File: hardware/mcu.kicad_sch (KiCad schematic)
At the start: 34 parts, among them J37 Micro_SD_Card, J38 Micro_SD_Card, U4 W25Q32JVZP, U5 RP2040, Y1 12 MHz ABM8-272-T3

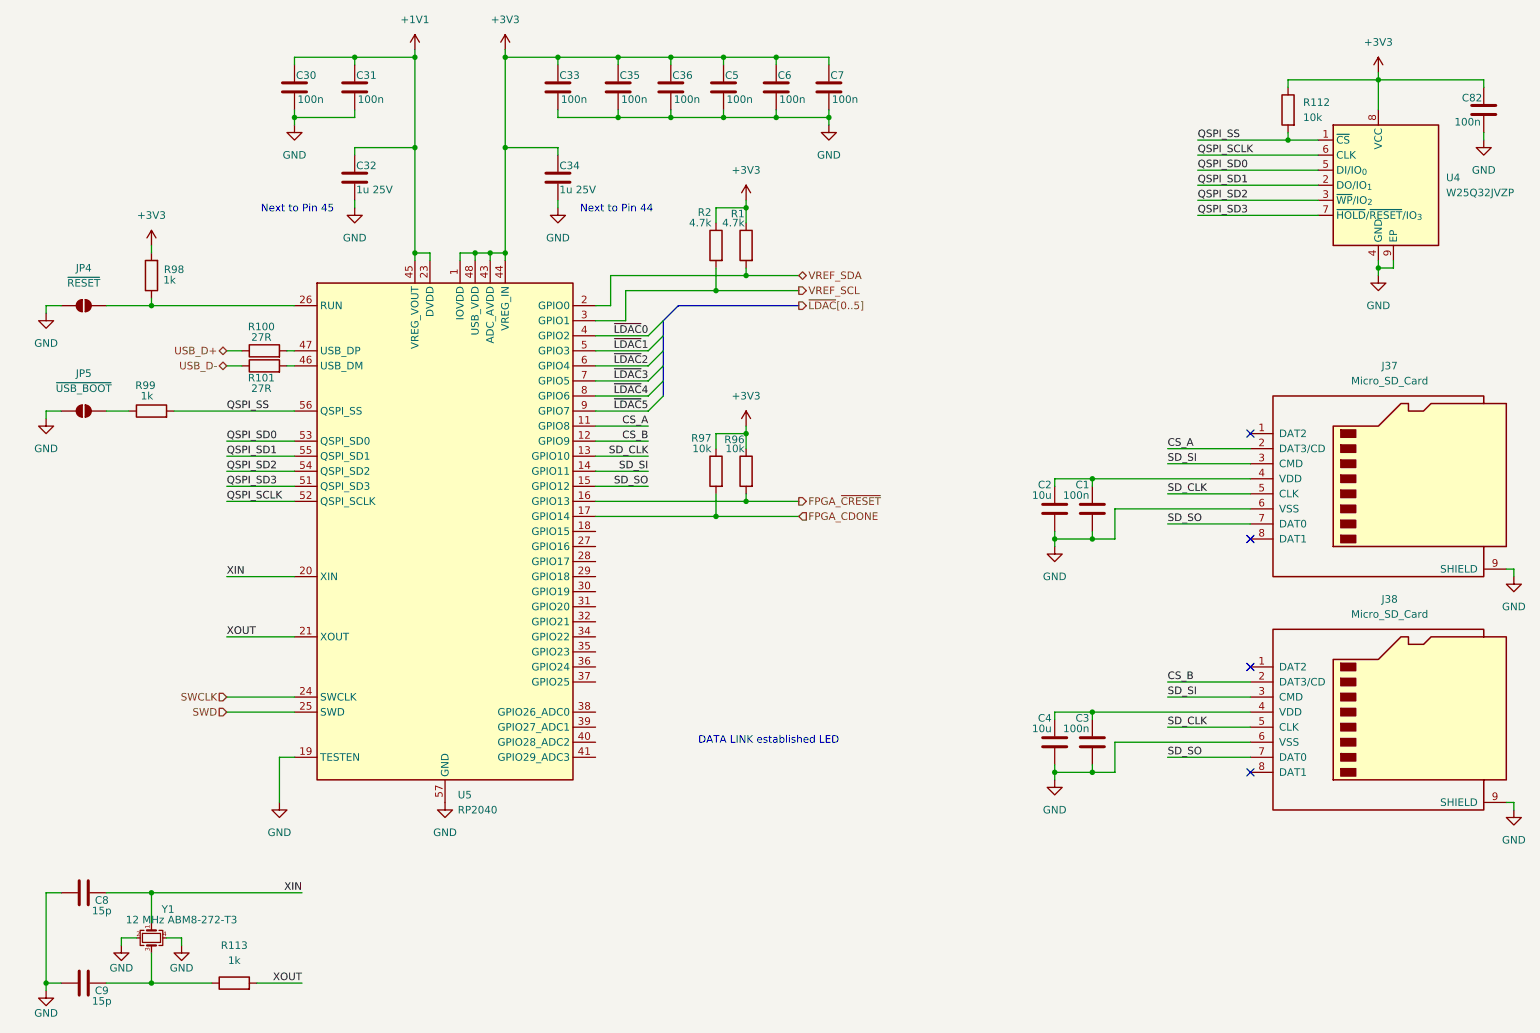
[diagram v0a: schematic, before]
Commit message: complete schematic wiring
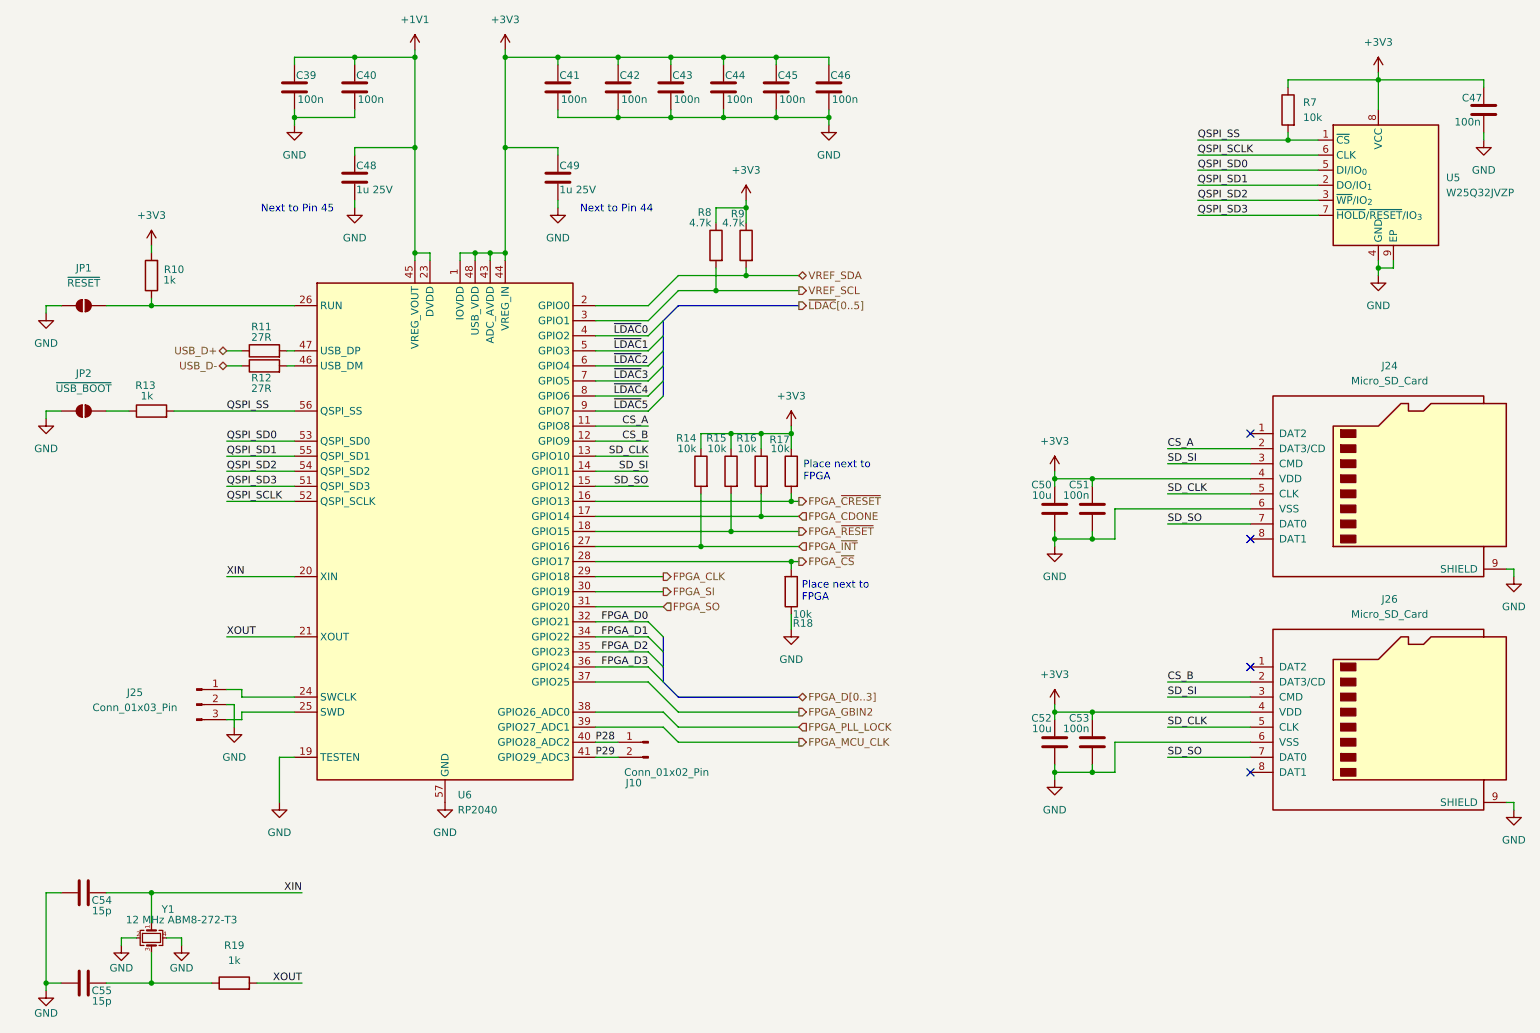
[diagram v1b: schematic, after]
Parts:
- added J10: Conn_01x02_Pin, symbol Connector:Conn_01x02_Pin
- added J25: Conn_01x03_Pin, symbol Connector:Conn_01x03_Pin
- added R14, R15, R18: 10k, symbol Device:R
- renumbered C30 to C39, C31 to C40, C33 to C41, C35 to C42, C36 to C43, C5 to C44, C6 to C45, C7 to C46, C82 to C47, C32 to C48, C34 to C49, C2 to C50, C1 to C51, C4 to C52, C3 to C53, C8 to C54, C9 to C55, J37 to J24, J38 to J26, JP4 to JP1, JP5 to JP2, R98 to R10, R100 to R11, R101 to R12, R99 to R13, R97 to R16, R96 to R17, R113 to R19, R112 to R7, R2 to R8, R1 to R9, U4 to U5, U5 to U6
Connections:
- net +3V3: now also C50.1, C51.1, C52.1, C53.1, J24.4 (VDD), J26.4 (VDD), R14.1, R15.1
- net GND: now also J25.2 (Pin_2), R18.1
- net FPGA_~{RESET}: now reaches U6.18 (GPIO15)
- net FPGA_~{RESET}: now also R15.2
- net FPGA_~{INT}: now reaches U6.27 (GPIO16)
- net FPGA_~{INT}: now also R14.2
- net FPGA_~{CS}: now reaches U6.28 (GPIO17)
- net FPGA_~{CS}: now also R18.2
- net FPGA_CLK: now reaches U6.29 (GPIO18)
- net FPGA_SI: now reaches U6.30 (GPIO19)
- net FPGA_SO: now reaches U6.31 (GPIO20)
- net FPGA_D0: now reaches U6.32 (GPIO21)
- net FPGA_D1: now reaches U6.34 (GPIO22)
- net FPGA_D2: now reaches U6.35 (GPIO23)
- net FPGA_D3: now reaches U6.36 (GPIO24)
- net FPGA_GBIN2: now reaches U6.37 (GPIO25)
- net FPGA_PLL_LOCK: now reaches U6.38 (GPIO26_ADC0)
- net FPGA_MCU_CLK: now reaches U6.39 (GPIO27_ADC1)
- net P28: now reaches U6.40 (GPIO28_ADC2)
- net P28: now also J10.1 (Pin_1)
- net P29: now reaches U6.41 (GPIO29_ADC3)
- net P29: now also J10.2 (Pin_2)
- net SWCLK: no longer names the net of U6.24 (SWCLK)
- net SWCLK: now also J25.1 (Pin_1)
- net SWD: no longer names the net of U6.25 (SWD)
- net SWD: now also J25.3 (Pin_3)
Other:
- note added: "Place next to FPGA"
- note removed: "DATA LINK established LED"
- moved on the sheet: R16, R17

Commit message: update power system + add LCSC part numbers
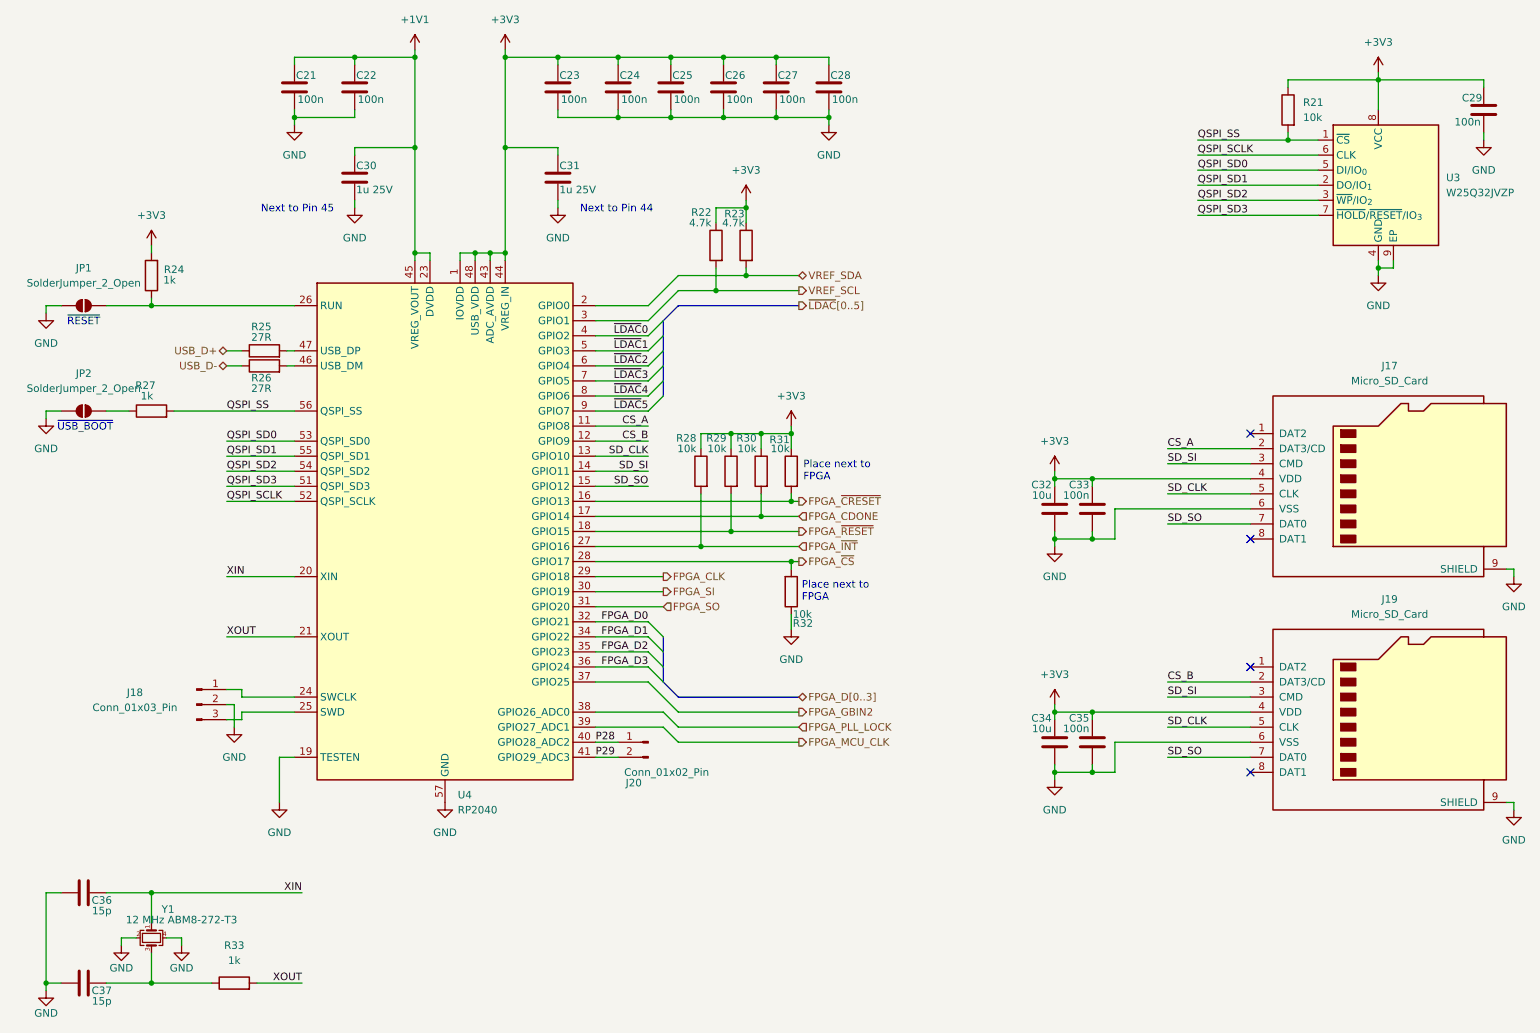
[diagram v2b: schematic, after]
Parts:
- C32: renamed from C50; footprint (none) -> Capacitor_SMD:C_1206_3216Metric; LCSC (none) -> C13585
- C33: renamed from C51; footprint (none) -> Capacitor_SMD:C_0402_1005Metric; LCSC (none) -> C307331
- C34: renamed from C52; footprint (none) -> Capacitor_SMD:C_1206_3216Metric; LCSC (none) -> C13585
- C35: renamed from C53; footprint (none) -> Capacitor_SMD:C_0402_1005Metric; LCSC (none) -> C307331
- J18: renamed from J25; footprint (none) -> Connector_PinHeader_2.54mm:PinHeader_1x03_P2.54mm_Vertical
- J20: renamed from J10; footprint (none) -> Connector_PinHeader_2.54mm:PinHeader_1x02_P2.54mm_Vertical
- JP1: value ~{RESET} -> SolderJumper_2_Open
- JP2: value ~{USB_BOOT} -> SolderJumper_2_Open
- R22: renamed from R8; footprint (none) -> Resistor_SMD:R_0402_1005Metric; LCSC (none) -> C25900
- R23: renamed from R9; footprint (none) -> Resistor_SMD:R_0402_1005Metric; LCSC (none) -> C25900
- R28: renamed from R14; footprint (none) -> Resistor_SMD:R_0402_1005Metric; LCSC (none) -> C25744
- R29: renamed from R15; footprint (none) -> Resistor_SMD:R_0402_1005Metric; LCSC (none) -> C25744
- R30: renamed from R16; footprint (none) -> Resistor_SMD:R_0402_1005Metric; LCSC (none) -> C25744
- R31: renamed from R17; footprint (none) -> Resistor_SMD:R_0402_1005Metric; LCSC (none) -> C25744
- R32: renamed from R18; footprint (none) -> Resistor_SMD:R_0402_1005Metric; LCSC (none) -> C25744
- U3: renamed from U5; LCSC (none) -> C571260
- renumbered C39 to C21, C40 to C22, C41 to C23, C42 to C24, C43 to C25, C44 to C26, C45 to C27, C46 to C28, C47 to C29, C48 to C30, C49 to C31, C54 to C36, C55 to C37, J24 to J17, J26 to J19, R7 to R21, R10 to R24, R11 to R25, R12 to R26, R13 to R27, R19 to R33, U6 to U4
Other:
- note added: "~{RESET}"
- note added: "~{USB_BOOT}"

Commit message: apply manufacturing BOM
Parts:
- removed J17, J19: Micro_SD_Card, symbol Connector:Micro_SD_Card
- removed J20: Conn_01x02_Pin, Connector_PinHeader_2.54mm:PinHeader_1x02_P2.54mm_Vertical, symbol Connector:Conn_01x02_Pin
- added J17, J19: Micro_SD_Card_Det1, digital:microSD_HC_MSD-4-A, symbol Connector:Micro_SD_Card_Det1
- added R32, R35: 10k, Resistor_SMD:R_0402_1005Metric, symbol Device:R
- added R33, R36: 0R, Resistor_SMD:R_0402_1005Metric, symbol Device:R
- renumbered R32 to R34, R33 to R37
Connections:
- net +3V3: now also J17.4 (VDD), J19.4 (VDD), R32.1, R35.1
- net CS_A: now also J17.2 (DAT3/CD)
- net CS_B: now also J19.2 (DAT3/CD)
- net GND: now also J17.10 (SHIELD), J17.6 (VSS), J19.10 (SHIELD), J19.6 (VSS)
- net SD_CLK: now also J17.5 (CLK), J19.5 (CLK)
- net SD_SI: now also J17.3 (CMD), J19.3 (CMD)
- net SD_SO: now also J17.7 (DAT0), J19.7 (DAT0)
- net P28 renamed DET_A
- net DET_A: now also R33.2
- net P29 renamed DET_B
- net DET_B: now also R36.2
- new net: J17.9 (DET), R32.2, R33.1
- new net: J19.9 (DET), R35.2, R36.1
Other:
- moved on the sheet: C32, C33, C34, C35

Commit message: route more
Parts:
- J18: footprint Connector_PinHeader_2.54mm:PinHeader_1x03_P2.54mm_Vertical -> Connector_PinHeader_1.00mm:PinHeader_1x03_P1.00mm_Vertical_SMD_Pin1Left
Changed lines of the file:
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@@
 			)
 		)
-		(property "Footprint" "Connector_PinHeader_2.54mm:PinHeader_1x03_P2.54mm_Vertical"
+		(property "Footprint" "Connector_PinHeader_1.00mm:PinHeader_1x03_P1.00mm_Vertical_SMD_Pin1Left"
 			(at 52.07 135.89 0)
 			(effects

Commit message: route mcu
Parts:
- J18: footprint Connector_PinHeader_1.00mm:PinHeader_1x03_P1.00mm_Vertical_SMD_Pin1Left -> Connector_PinHeader_2.54mm:PinHeader_1x03_P2.54mm_Vertical
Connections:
- net D-: now reaches R26.2, U4.46 (USB_DM)
- net D+: now reaches R25.2, U4.47 (USB_DP)
- net SWCLK: now reaches J18.1 (Pin_1), U4.24 (SWCLK)
- net SWD: now reaches J18.3 (Pin_3), U4.25 (SWD)
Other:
- moved on the sheet: J18, R25, R26
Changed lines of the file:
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@@
 	(wire
 		(pts
-			(xy 59.69 134.62) (xy 59.69 133.35)
+			(xy 57.15 134.62) (xy 57.15 133.35)
 		)
 		(stroke
@@
 	(wire
 		(pts
-			(xy 58.42 135.89) (xy 58.42 139.7)
+			(xy 55.88 135.89) (xy 55.88 139.7)
 		)
 		(stroke
@@
 	(wire
 		(pts
-			(xy 59.69 76.2) (xy 57.15 76.2)
+			(xy 58.42 76.2) (xy 55.88 76.2)
 		)
 		(stroke
@@
 	(wire
 		(pts
-			(xy 67.31 76.2) (xy 68.58 76.2)
+			(xy 66.04 76.2) (xy 68.58 76.2)
 		)
 		(stroke
@@
 	(wire
 		(pts
-			(xy 57.15 135.89) (xy 58.42 135.89)
+			(xy 54.61 135.89) (xy 55.88 135.89)
 		)
 		(stroke
@@
 	(wire
 		(pts
-			(xy 59.69 137.16) (xy 68.58 137.16)
+			(xy 57.15 137.16) (xy 68.58 137.16)
 		)
 		(stroke
@@
 	(wire
 		(pts
-			(xy 59.69 78.74) (xy 57.15 78.74)
+			(xy 58.42 78.74) (xy 55.88 78.74)
 		)
 		(stroke
@@
 	(wire
 		(pts
-			(xy 59.69 138.43) (xy 57.15 138.43)
+			(xy 57.15 138.43) (xy 54.61 138.43)
 		)
 		(stroke
@@
 	(wire
 		(pts
-			(xy 59.69 137.16) (xy 59.69 138.43)
+			(xy 57.15 137.16) (xy 57.15 138.43)
 		)
 		(stroke
@@
 	(wire
 		(pts
-			(xy 67.31 78.74) (xy 68.58 78.74)
+			(xy 66.04 78.74) (xy 68.58 78.74)
 		)
 		(stroke
@@
 	(wire
 		(pts
-			(xy 68.58 134.62) (xy 59.69 134.62)
-		)
-		(stroke
-			(width 0)
-			(type default)
-		)
-	)
-	(wire
-		(pts
 			(xy 128.27 76.2) (xy 119.38 76.2)
 		)
@@
 	(wire
 		(pts
-			(xy 59.69 133.35) (xy 57.15 133.35)
+			(xy 57.15 133.35) (xy 54.61 133.35)
 		)
 		(stroke
@@
 	(wire
 		(pts
+			(xy 57.15 134.62) (xy 68.58 134.62)
+		)
+		(stroke
+			(width 0)
+			(type default)
+		)
+	)
+	(wire
+		(pts
 			(xy 128.27 99.06) (xy 119.38 99.06)
 		)
@@
 		)
 	)
+	(label "D+"
+		(at 66.04 76.2 0)
+		(effects
+			(font
+				(size 1.27 1.27)
+			)
+			(justify left bottom)
+		)
+	)
 	(label "~{LDAC}5"
 		(at 128.27 86.36 180)
@@
 		)
 	)
+	(label "SWCLK"
+		(at 57.15 134.62 0)
+		(effects
+			(font
+				(size 1.27 1.27)
+			)
+			(justify left bottom)
+		)
+	)
 	(label "QSPI_SD2"
 		(at 57.15 96.52 0)
@@
 		)
 	)
+	(label "SWD"
+		(at 57.15 137.16 0)
+		(effects
+			(font
+				(size 1.27 1.27)
+			)
+			(justify left bottom)
+		)
+	)
 	(label "FPGA_D1"
 		(at 128.27 124.46 180)
@@
 		)
 	)
+	(label "D-"
+		(at 66.04 78.74 0)
+		(effects
+			(font
+				(size 1.27 1.27)
+			)
+			(justify left bottom)
+		)
+	)
 	(label "SD_SI"
 		(at 215.9 95.25 0)
@@
 	(hierarchical_label "USB_D-"
 		(shape bidirectional)
-		(at 57.15 78.74 180)
+		(at 55.88 78.74 180)
 		(effects
 			(font
@@
 	(hierarchical_label "USB_D+"
 		(shape bidirectional)
-		(at 57.15 76.2 180)
+		(at 55.88 76.2 180)
 		(effects
 			(font
@@
 		)
 	)
+	(rule_area
+		(polyline
+			(pts
+				(xy 45.72 71.12) (xy 45.72 83.185) (xy 71.12 83.185) (xy 71.12 71.12)
+			)
+			(stroke
+				(width 0)
+				(type dash)
+			)
+			(fill
+				(type none)
+			)
+		)
+	)
+	(netclass_flag ""
+		(length 2.54)
+		(shape round)
+		(at 45.72 77.47 90)
+		(effects
+			(font
+				(size 1.27 1.27)
+			)
+			(justify left bottom)
+		)
+		(property "Netclass" "USB"
+			(at 38.354 77.47 0)
+			(effects
+				(font
+					(size 1.27 1.27)
+				)
+				(justify left)
+			)
+		)
+		(property "Component Class" ""
+			(at -34.29 3.81 0)
+			(effects
+				(font
+					(size 1.27 1.27)
+					(italic yes)
+				)
+			)
+		)
+	)
 	(symbol
 		(lib_id "Device:R")
@@
 	(symbol
 		(lib_id "Device:R")
-		(at 63.5 78.74 90)
+		(at 62.23 78.74 90)
 		(unit 1)
 		(exclude_from_sim no)
@@
 		(dnp no)
 		(property "Reference" "R26"
-			(at 62.992 80.772 90)
+			(at 61.722 80.772 90)
 			(effects
 				(font
@@
 		)
 		(property "Value" "27R"
-			(at 62.992 82.55 90)
+			(at 61.722 82.55 90)
 			(effects
 				(font
@@
 		)
 		(property "Footprint" "Resistor_SMD:R_0402_1005Metric"
-			(at 63.5 80.518 90)
+			(at 62.23 80.518 90)
 			(effects
 				(font
@@
 		)
 		(property "Datasheet" "~"
-			(at 63.5 78.74 0)
+			(at 62.23 78.74 0)
 			(effects
 				(font
@@
 		)
 		(property "Description" "Resistor"
-			(at 63.5 78.74 0)
+			(at 62.23 78.74 0)
 			(effects
 				(font
@@
 		)
 		(property "LCSC" "C138021"
-			(at 63.5 78.74 90)
+			(at 62.23 78.74 90)
 			(effects
 				(font
@@
 	(symbol
 		(lib_id "Device:R")
-		(at 63.5 76.2 90)
+		(at 62.23 76.2 90)
 		(unit 1)
 		(exclude_from_sim no)
@@
 		(dnp no)
 		(property "Reference" "R25"
-			(at 62.992 72.136 90)
+			(at 61.722 72.136 90)
 			(effects
 				(font
@@
 		)
 		(property "Value" "27R"
-			(at 62.992 73.914 90)
+			(at 61.722 73.914 90)
 			(effects
 				(font
@@
 		)
 		(property "Footprint" "Resistor_SMD:R_0402_1005Metric"
-			(at 63.5 77.978 90)
+			(at 62.23 77.978 90)
 			(effects
 				(font
@@
 		)
 		(property "Datasheet" "~"
-			(at 63.5 76.2 0)
+			(at 62.23 76.2 0)
 			(effects
 				(font
@@
 		)
 		(property "Description" "Resistor"
-			(at 63.5 76.2 0)
+			(at 62.23 76.2 0)
 			(effects
 				(font
@@
 		)
 		(property "LCSC" "C138021"
-			(at 63.5 76.2 90)
+			(at 62.23 76.2 90)
 			(effects
 				(font
@@
 	(symbol
 		(lib_id "power:GND")
-		(at 58.42 139.7 0)
+		(at 55.88 139.7 0)
 		(unit 1)
 		(exclude_from_sim no)
@@
 		(fields_autoplaced yes)
 		(property "Reference" "#PWR040"
-			(at 58.42 146.05 0)
+			(at 55.88 146.05 0)
 			(effects
 				(font
@@
 		)
 		(property "Value" "GND"
-			(at 58.42 144.78 0)
+			(at 55.88 144.78 0)
 			(effects
 				(font
@@
 		)
 		(property "Footprint" ""
-			(at 58.42 139.7 0)
+			(at 55.88 139.7 0)
 			(effects
 				(font
@@
 		)
 		(property "Datasheet" ""
-			(at 58.42 139.7 0)
+			(at 55.88 139.7 0)
 			(effects
 				(font
@@
 		)
 		(property "Description" "Power symbol creates a global label with name \"GND\" , ground"
-			(at 58.42 139.7 0)
+			(at 55.88 139.7 0)
 			(effects
 				(font
@@
 	(symbol
 		(lib_id "Connector:Conn_01x03_Pin")
-		(at 52.07 135.89 0)
+		(at 49.53 135.89 0)
 		(unit 1)
 		(exclude_from_sim no)
@@
 		(dnp no)
 		(property "Reference" "J18"
-			(at 41.656 133.858 0)
+			(at 39.116 133.858 0)
 			(effects
 				(font
@@
 		)
 		(property "Value" "Conn_01x03_Pin"
-			(at 41.656 136.398 0)
+			(at 39.116 136.398 0)
 			(effects
 				(font
@@
 			)
 		)
-		(property "Footprint" "Connector_PinHeader_1.00mm:PinHeader_1x03_P1.00mm_Vertical_SMD_Pin1Left"
-			(at 52.07 135.89 0)
+		(property "Footprint" "Connector_PinHeader_2.54mm:PinHeader_1x03_P2.54mm_Vertical"
+			(at 49.53 135.89 0)
 			(effects
 				(font
@@
 		)
 		(property "Datasheet" "~"
-			(at 52.07 135.89 0)
+			(at 49.53 135.89 0)
 			(effects
 				(font
@@
 		)
 		(property "Description" "Generic connector, single row, 01x03, script generated"
-			(at 52.07 135.89 0)
+			(at 49.53 135.89 0)
 			(effects
 				(font
